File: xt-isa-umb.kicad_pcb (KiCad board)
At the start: 2 copper layers, 94 x 60.5 mm, 15 parts, among them J1 Bus_ISA_8bit, U1 74LS138, U2 74LS08, U3 AS6C1008, U4 74HCT245

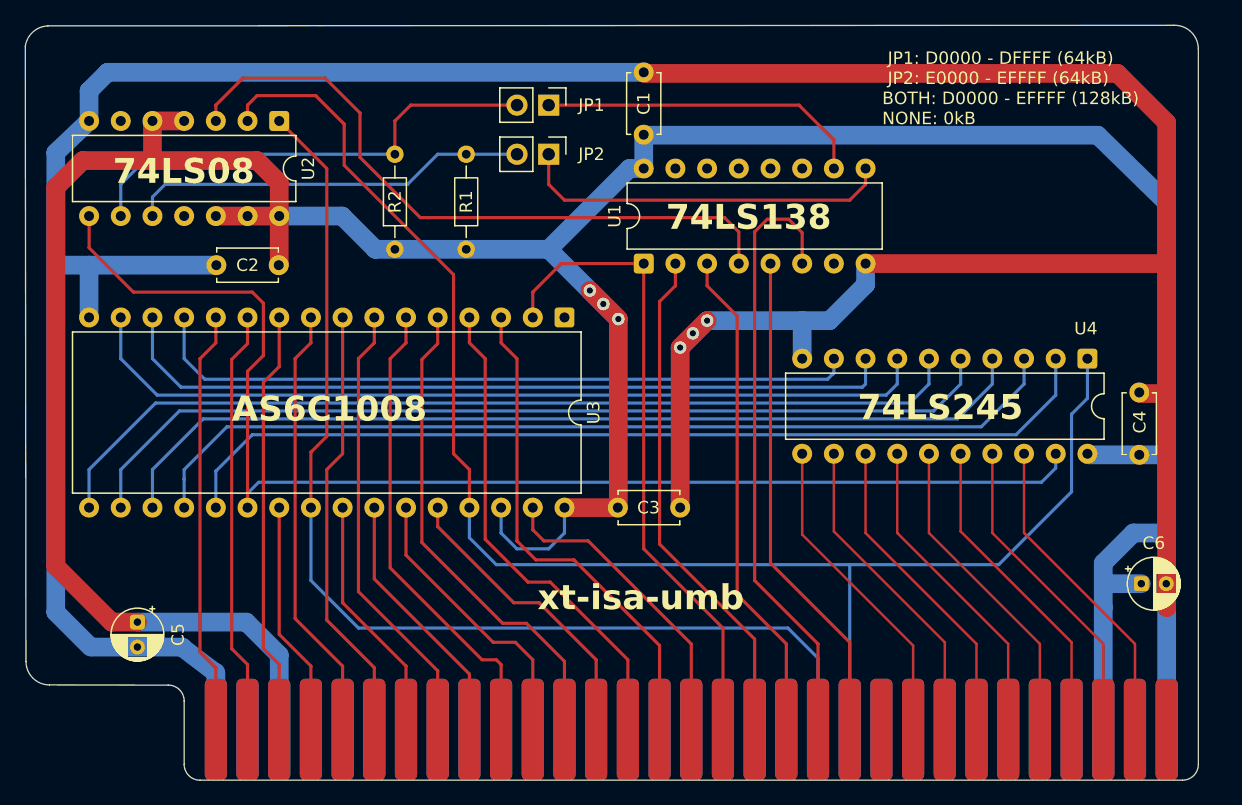
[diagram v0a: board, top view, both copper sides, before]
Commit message: Modify capacitors and VCC/GND track placement
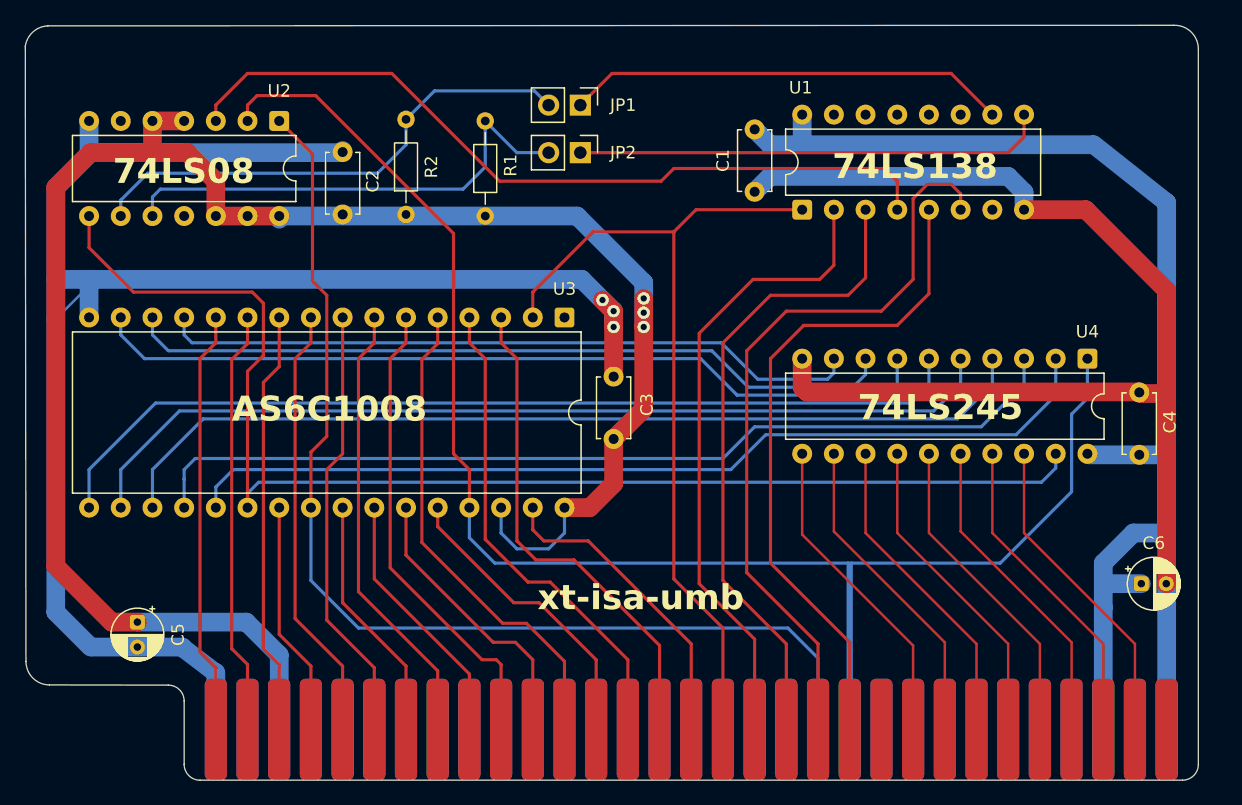
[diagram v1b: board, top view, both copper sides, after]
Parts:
- moved U1 13.4 mm to (148.6, 98.6)
- moved C1 8.90 mm to (144.8, 92.1), turned to -90 degrees
- moved C2 6.54 mm to (111.8, 98.9), turned to 90 degrees
- moved C3 5.51 mm to (133.5, 116.9), turned to 90 degrees
- moved R1 3.07 mm to (123.2, 99.1)
- moved R2 2.93 mm to (116.8, 98.9)
- moved JP2 2.54 mm to (130.8, 94.0)
- moved JP1 2.53 mm to (130.8, 90.2)
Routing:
- net GND: track 186.8 -> 215.1 mm
- net /A16: track 51.8 -> 68.2 mm
- net Net-(J1-AEN): track 40.0 -> 53.6 mm
- net VCC: track 223.1 -> 236.4 mm
- net /A18: track 40.0 -> 52.1 mm
- net /A19: track 49.3 -> 60.8 mm
- net /A17: track 41.0 -> 51.1 mm
- net Net-(U1-E1): track 54.1 -> 63.9 mm
- net Net-(JP1-A): track 26.3 -> 35.8 mm
- net Net-(JP1-B): track 33.6 -> 40.9 mm
- net Net-(JP2-A): track 30.3 -> 37.5 mm
- net Net-(JP2-B): track 32.4 -> 39.4 mm
- net Net-(U3-DQ1): track 63.5 -> 62.0 mm
- net Net-(U3-DQ0): track 57.6 -> 56.3 mm
- net Net-(U3-DQ2): track 69.1 -> 68.0 mm
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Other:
- board text removed: "JP1: D0000 - DFFFF (64kB) JP2: E0000 - EFFFF (64kB) BOTH: D0000 - EFFFF (128kB) NONE: 0kB"

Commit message: Further VCC/GND tracks modification
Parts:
- removed C5: 47uF, Capacitor_THT:CP_Radial_D4.0mm_P2.00mm
- moved JP1 3.90 mm to (134.5, 88.9)
- moved JP2 3.56 mm to (134.4, 94.0)
- moved C2 1.27 mm to (110.5, 99.0)
- moved C1 1.18 mm to (144.8, 90.9)
- moved R2 0.13 mm to (116.8, 99.1)
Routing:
- net GND: track 215.1 -> 284.1 mm
- net /A6: track 0.00 -> 19.9 mm
- net /A16: track 68.2 -> 76.5 mm
- net VCC: track 236.4 -> 232.2 mm
- net Net-(JP2-A): track 37.5 -> 34.3 mm
- net Net-(JP1-A): track 35.8 -> 32.8 mm
- net /MEMR: track 87.9 -> 85.3 mm
- net Net-(JP1-B): track 40.9 -> 43.1 mm
- net Net-(JP2-B): track 39.4 -> 41.0 mm
- net Net-(U1-E1): track 63.9 -> 64.6 mm
- net /A10: track 23.0 -> 22.4 mm
- net /A9: track 37.9 -> 37.2 mm
- net /A14: track 40.1 -> 39.4 mm
- net /A11: track 43.0 -> 42.4 mm
- net /A12: track 24.2 -> 23.7 mm
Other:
- board text added: "JP1: 64kB (D0000 - DFFFF) JP2: 64kB (E0000 - EFFFF) BOTH: 128kB (D0000 - EFFFF) NONE: 0kB"

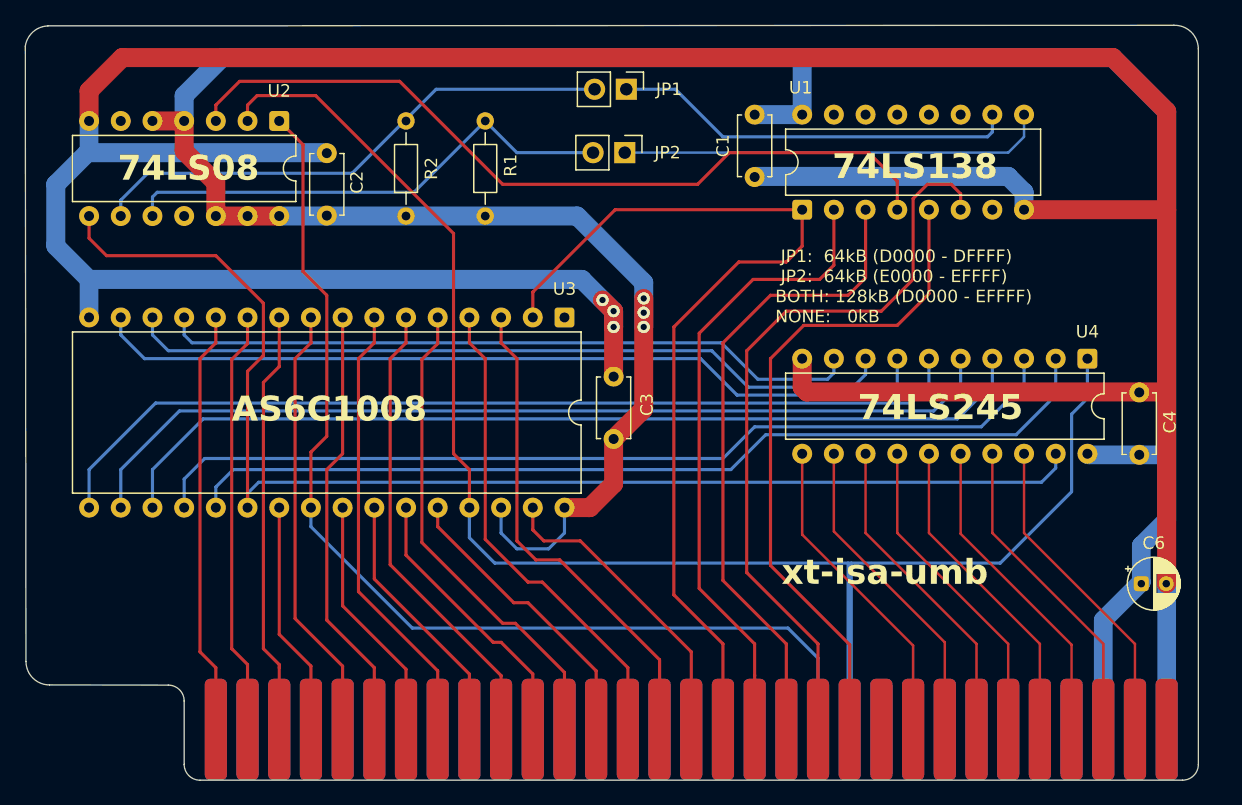
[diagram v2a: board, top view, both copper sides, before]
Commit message: Add GND fill zone.
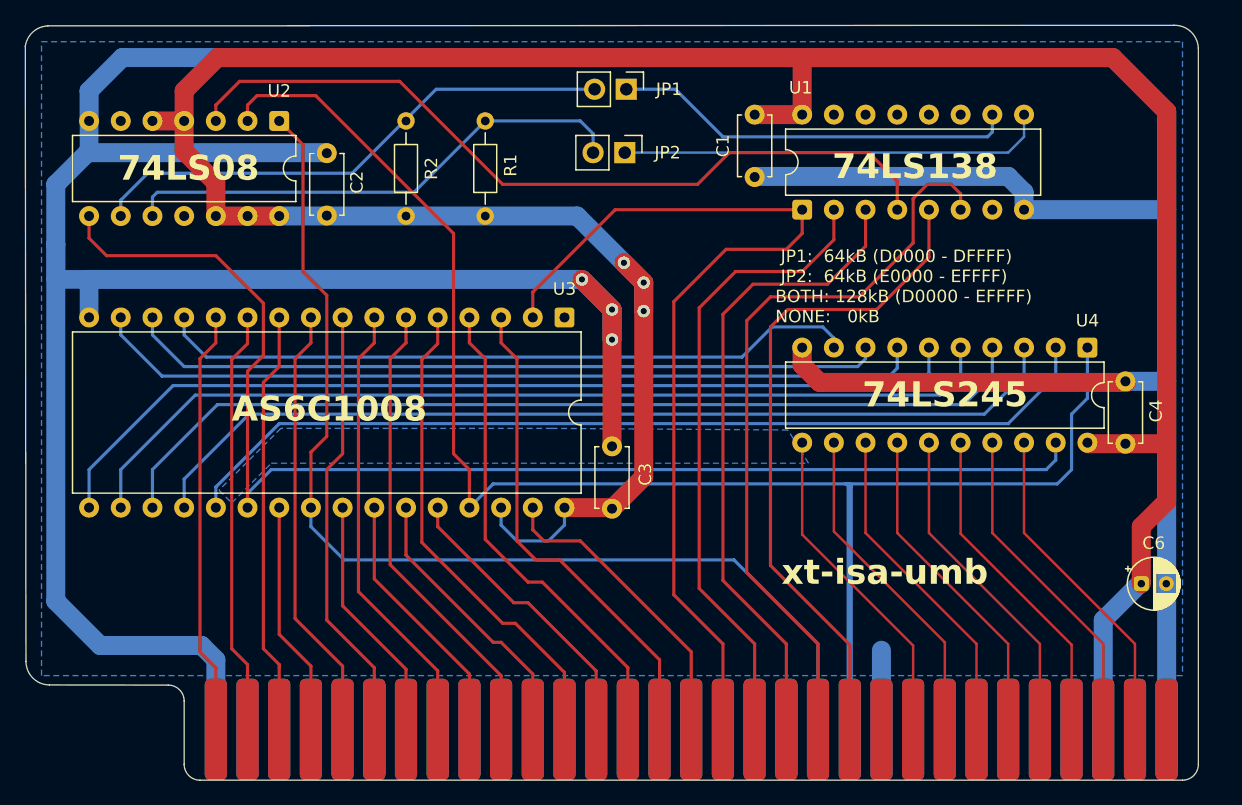
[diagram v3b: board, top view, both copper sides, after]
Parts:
- moved C3 5.59 mm to (133.3, 122.5)
- moved C4 1.42 mm to (174.5, 117.3)
- moved U4 0.89 mm to (171.4, 109.6)
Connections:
- J1 pad 29: VCC -> unconnected-(J1-VCC-Pad29)
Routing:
- net GND: track 284.1 -> 361.1 mm
- net /MEMW: track 123.6 -> 130.8 mm
- net VCC: track 232.2 -> 234.7 mm
- net Net-(U3-DQ1): track 62.0 -> 60.8 mm
- net Net-(U3-DQ2): track 68.0 -> 66.9 mm
- net Net-(JP2-B): track 41.0 -> 41.9 mm
- net /D6: track 25.8 -> 26.7 mm
- net /D5: track 25.8 -> 26.7 mm
- net /D4: track 25.8 -> 26.7 mm
- net /D3: track 25.8 -> 26.7 mm
- net /D2: track 25.8 -> 26.7 mm
- net /D1: track 25.8 -> 26.7 mm
- net /D0: track 25.8 -> 26.7 mm
- net /MEMR: track 85.3 -> 86.0 mm
- net /A16: track 76.5 -> 77.1 mm
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- added copper zone on B.Cu, net GND

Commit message: Add top GND fill zone
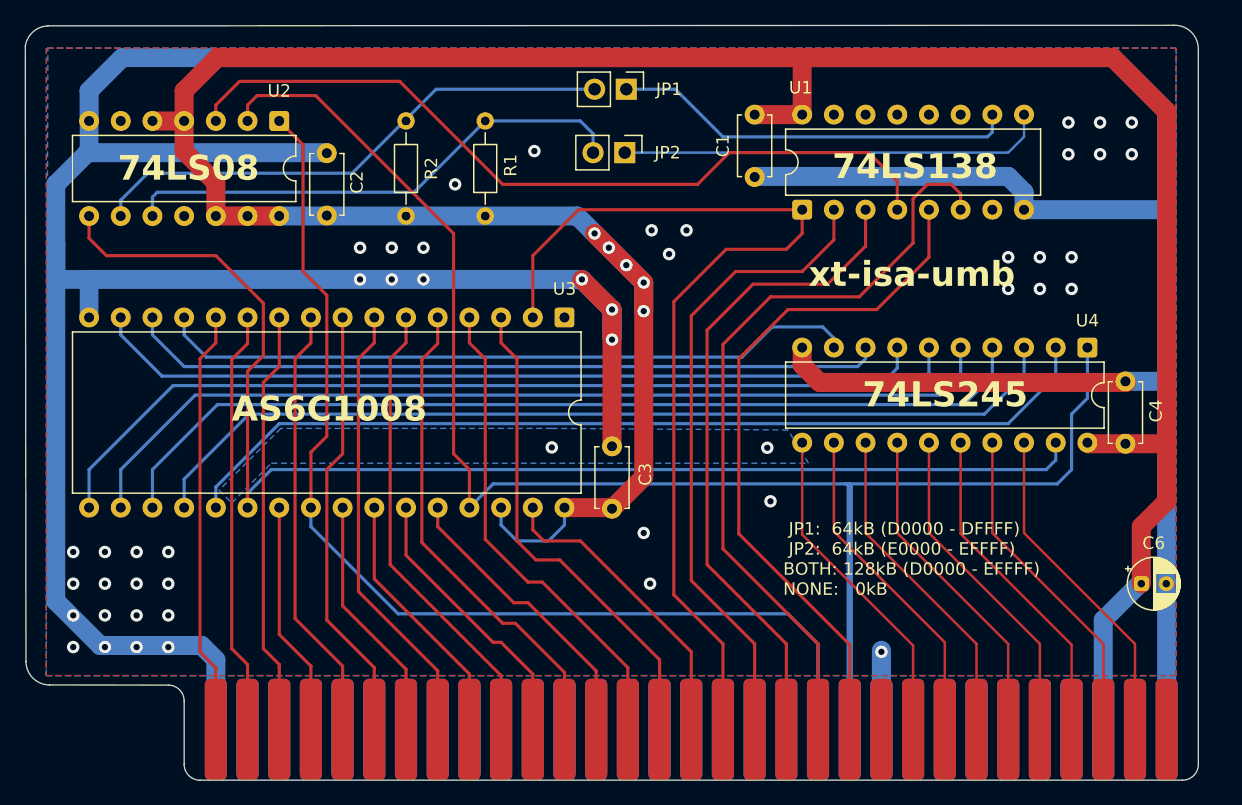
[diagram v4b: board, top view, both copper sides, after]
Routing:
- net VCC: track 234.7 -> 238.1 mm, vias 3 -> 5
- net Net-(J1-AEN): track 53.3 -> 55.4 mm
- net /A16: track 77.1 -> 78.8 mm
- net /A19: track 60.5 -> 62.0 mm
- net /A18: track 52.0 -> 53.0 mm
- net /A17: track 51.1 -> 51.6 mm
- net GND: vias 3 -> 48
- added copper zone on F.Cu, net GND
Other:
- board text removed: "[zyga64]"

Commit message: Add gerber files
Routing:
- net /MEMW: track 130.8 -> 125.0 mm
- net GND: vias 48 -> 52
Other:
- board text added: "https://github.com/zyga64/xt-isa-umb"
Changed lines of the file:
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@@
 			(plot_on_all_layers_selection 0x00000000_00000000_00000000_00000000)
 			(disableapertmacros no)
-			(usegerberextensions no)
+			(usegerberextensions yes)
 			(usegerberattributes yes)
 			(usegerberadvancedattributes yes)
@@
 			(outputformat 1)
 			(mirror no)
-			(drillshape 1)
+			(drillshape 0)
 			(scaleselection 1)
-			(outputdirectory "")
+			(outputdirectory "gerbers/")
 		)
 	)
@@
 			(net 63 "unconnected-(U1-O7-Pad7)")
 			(pinfunction "O7")
-			(pintype "output")
+			(pintype "output+no_connect")
 		)
 		(pad "8" thru_hole circle
@@
 			(net 64 "unconnected-(U1-O4-Pad11)")
 			(pinfunction "O4")
-			(pintype "output")
+			(pintype "output+no_connect")
 		)
 		(pad "12" thru_hole circle
@@
 			(net 60 "unconnected-(U1-O3-Pad12)")
 			(pinfunction "O3")
-			(pintype "output")
+			(pintype "output+no_connect")
 		)
 		(pad "13" thru_hole circle
@@
 			(net 65 "unconnected-(U1-O2-Pad13)")
 			(pinfunction "O2")
-			(pintype "output")
+			(pintype "output+no_connect")
 		)
 		(pad "14" thru_hole circle
@@
 			(net 66 "unconnected-(U1-O1-Pad14)")
 			(pinfunction "O1")
-			(pintype "output")
+			(pintype "output+no_connect")
 		)
 		(pad "15" thru_hole circle
@@
 			(net 61 "unconnected-(U1-O0-Pad15)")
 			(pinfunction "O0")
-			(pintype "output")
+			(pintype "output+no_connect")
 		)
 		(pad "16" thru_hole circle
@@
 			(remove_unused_layers no)
 			(net 78 "unconnected-(U2-Pad6)")
-			(pintype "output")
+			(pintype "output+no_connect")
 		)
 		(pad "7" thru_hole circle
@@
 			(remove_unused_layers no)
 			(net 77 "unconnected-(U2-Pad11)")
-			(pintype "output")
+			(pintype "output+no_connect")
 		)
 		(pad "12" thru_hole circle
@@
 	)
 	(gr_text " JP1:  64kB (D0000 - DFFFF)\n JP2:  64kB (E0000 - EFFFF)\nBOTH: 128kB (D0000 - EFFFF)\nNONE:   0kB"
-		(at 147.066 129.54 0)
+		(at 142.621 131.445 0)
 		(layer "F.SilkS")
 		(effects
@@
 		)
 	)
+	(gr_text "https://github.com/zyga64/xt-isa-umb"
+		(at 119.888 134.62 0)
+		(layer "B.SilkS")
+		(effects
+			(font
+				(size 1 1)
+				(thickness 0.1)
+			)
+			(justify left bottom mirror)
+		)
+	)
 	(segment
 		(start 133.35 106.553)
@@
 	)
 	(via
+		(at 172.847 122.682)
+		(size 1)
+		(drill 0.5)
+		(layers "F.Cu" "B.Cu")
+		(net 3)
+	)
+	(via
 		(at 90.17 128.524)
 		(size 1)
@@
 	)
 	(via
+		(at 170.307 122.682)
+		(size 1)
+		(drill 0.5)
+		(layers "F.Cu" "B.Cu")
+		(net 3)
+	)
+	(via
+		(at 172.847 125.222)
+		(size 1)
+		(drill 0.5)
+		(layers "F.Cu" "B.Cu")
+		(net 3)
+	)
+	(via
 		(at 137.922 102.108)
 		(size 1)
@@
 	)
 	(via
+		(at 170.307 125.222)
+		(size 1)
+		(drill 0.5)
+		(layers "F.Cu" "B.Cu")
+		(net 3)
+	)
+	(via
 		(at 167.64 104.902)
 		(size 1)
@@
 		(width 0.254)
 		(layer "B.Cu")
-		(net 7)
-	)
-	(segment
-		(start 152.4 120.65)
-		(end 152.4 126.492001)
-		(width 0.254)
-		(layer "B.Cu")

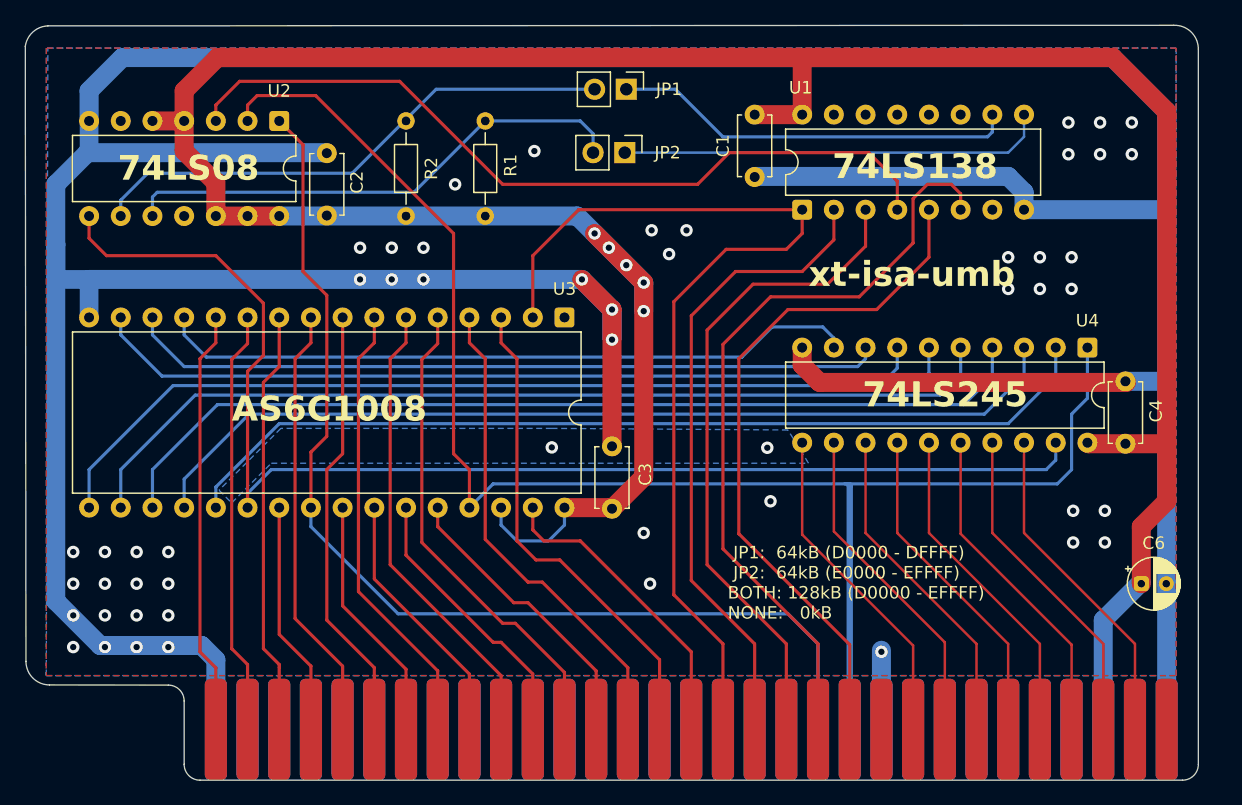
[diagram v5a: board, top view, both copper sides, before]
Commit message: Modify components designation, add thermal reliefs, change C6 orientation
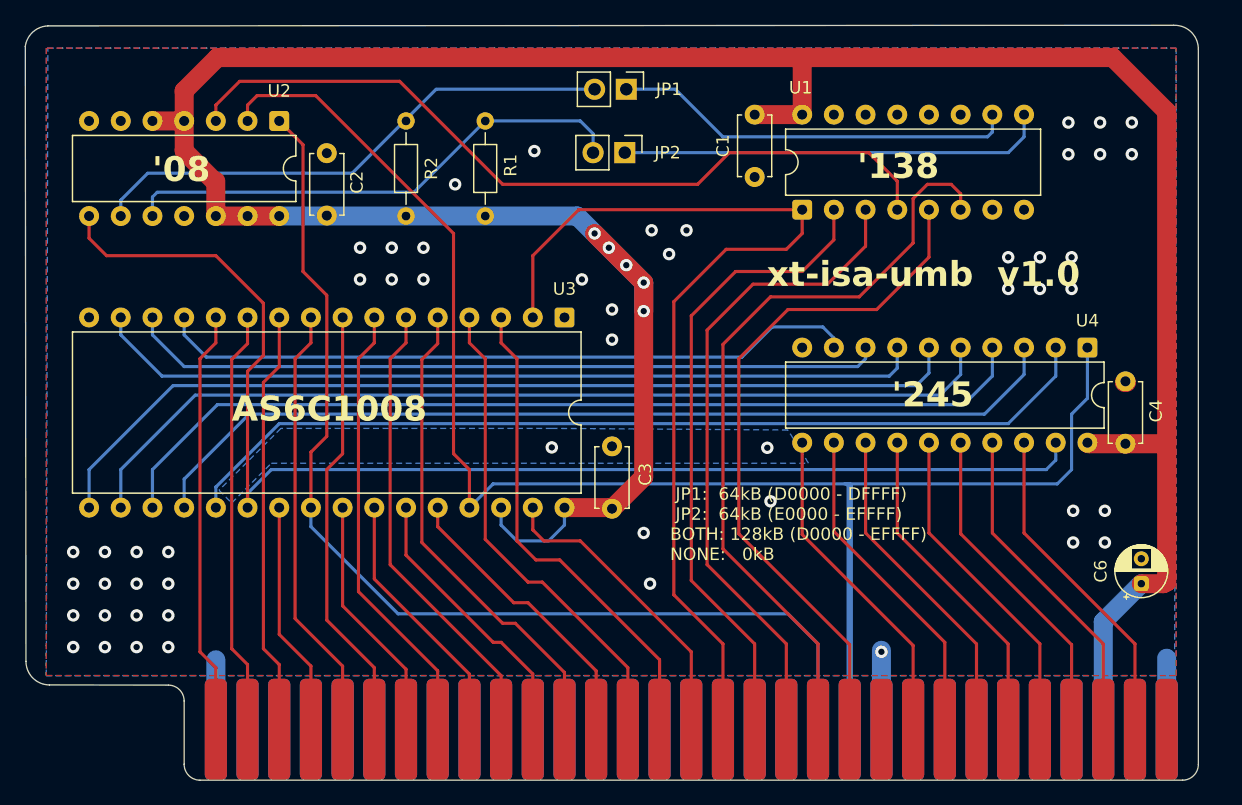
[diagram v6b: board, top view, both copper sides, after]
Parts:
- turned C6 to 90 degrees
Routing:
- net GND: track 361.1 -> 18.0 mm
- net /A11: track 42.4 -> 38.9 mm
- net VCC: track 238.1 -> 239.0 mm
- net /D7: track 25.8 -> 26.7 mm
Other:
- board text added: "'08"
- board text added: "'138"
- board text added: "'245"
- board text added: "xt-isa-umb v1.0"
- board text removed: "74LS08"
- board text removed: "74LS138"
- board text removed: "74LS245"
- board text removed: "xt-isa-umb"
